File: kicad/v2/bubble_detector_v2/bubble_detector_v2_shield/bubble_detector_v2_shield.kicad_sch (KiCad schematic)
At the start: 9 parts, among them J1 Power, J2 Digital/PWM, J3 Analog, J4 Digital/PWM, U1 HC-SR04

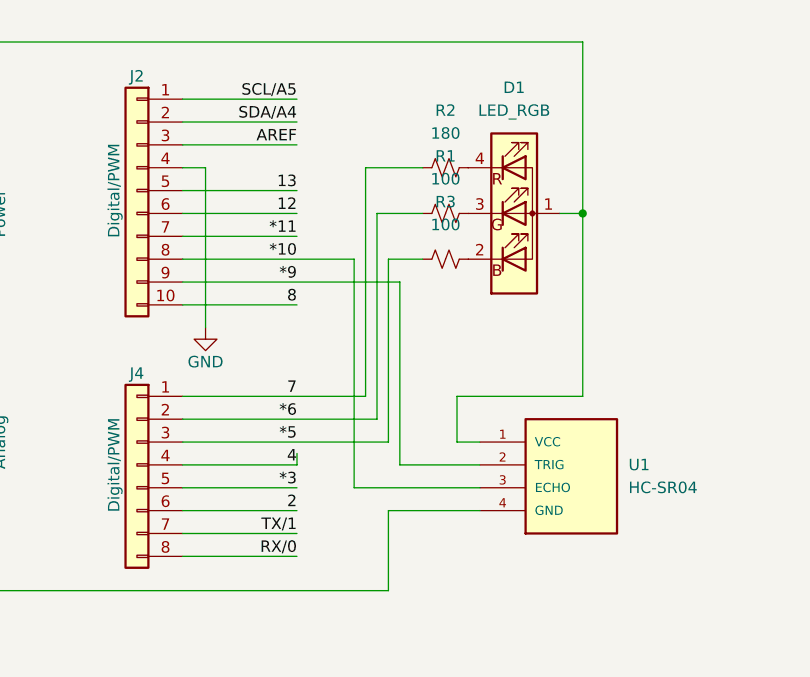
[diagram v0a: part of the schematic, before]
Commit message: missing edge cut
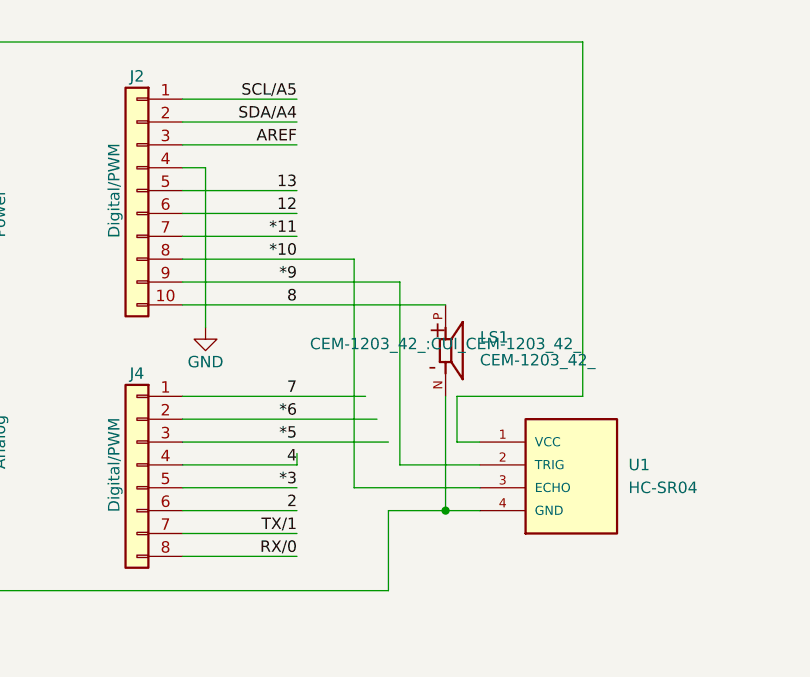
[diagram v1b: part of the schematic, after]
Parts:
- removed D1: LED_RGB, SparkFun-LED:LED_1205_RGB_Bottom, symbol SparkFun-LED:LED_RGB_1205_Bottom
- removed R1, R3: 100, SparkFun-Resistor:R_0402_1005Metric, symbol SparkFun-Resistor:100_0402
- removed R2: 180, SparkFun-Resistor:R_0603_1608Metric, symbol SparkFun-Resistor:180_0603
- added LS1: CEM-1203_42_, CEM-1203_42_:CUI_CEM-1203_42_, symbol CEM-1203_42_:CEM-1203_42_
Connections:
- net 8: now also LS1.P
- net GND: now also LS1.N
